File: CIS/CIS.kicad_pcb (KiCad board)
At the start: 8 copper layers, 88 parts, among them K1 K_0043, P1 K_0021, P2 K_0021, P7 K_0021, U1 U_0005, U10 U_0049, U11 U_0049, U14 U_0101, U15 U_0005, U16 U_0049, U17 U_0049, U2 STM32H745IIKx, U8 U_0049, U9 U_0049

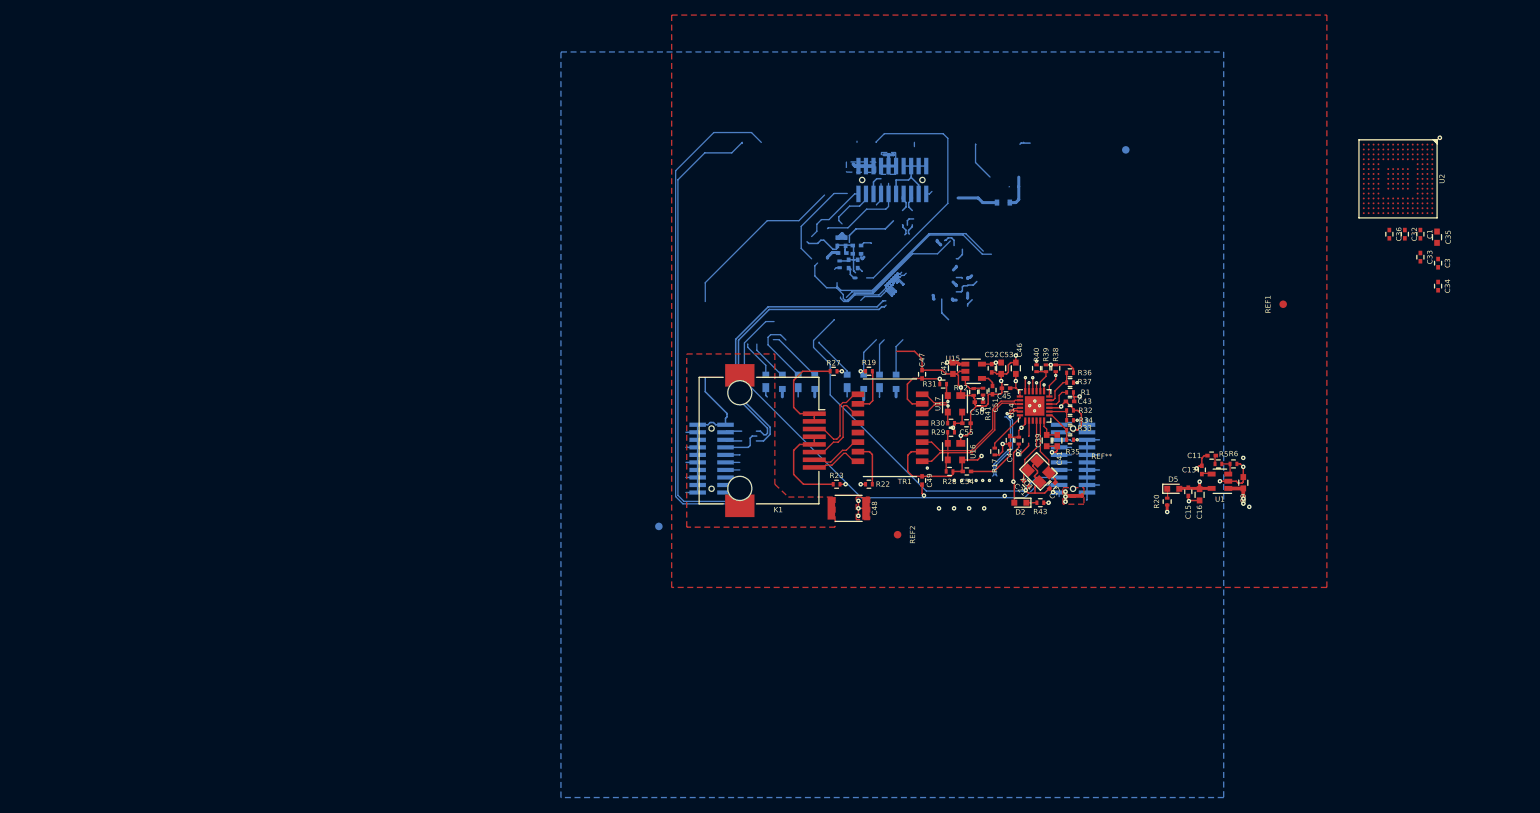
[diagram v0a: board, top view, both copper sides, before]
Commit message: Place components and route POWER + ETHERNET
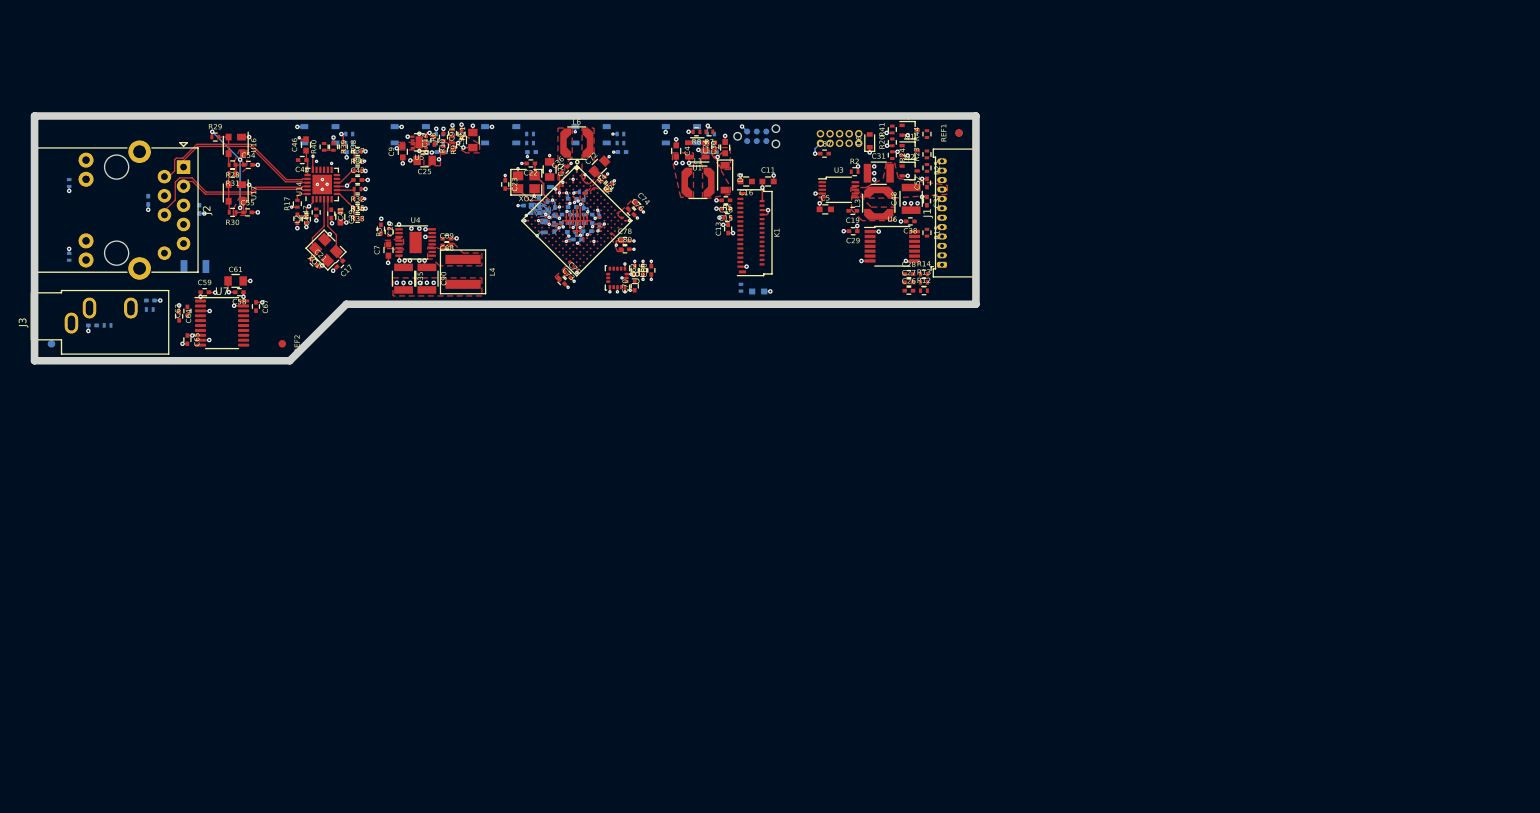
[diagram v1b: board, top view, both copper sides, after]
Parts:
- removed C50: C_0002, DVB_Capacitors_Ceramic:C_0402
- removed C51: C_0001, DVB_Capacitors_Ceramic:C_0402
- removed D5: D_0001, DVB_LED:LED_0603-red
- removed P1, P2, P7: K_0021, DVB_Connectors:K_MLE-110-01-G-DV-A
- removed REF**: VAL**, DVB_Mechanicals:DVBLOGO
- removed TR1: TR_0001, DVB_Transfo:LAN_8-13x7_P1.27
- removed U10, U11, U9: U_0049, DVB_SOT:SOT_143
- removed U15: U_0005, DVB_SOT:SOT_23-5
- added C14: C_0002, DVB_Capacitors_Ceramic:C_0402, F.Cu at (94.2, 75.8)
- added C18: C_0044, DVB_Capacitors_Ceramic:C_0402, F.Cu at (132.9, 83.7)
- added C19: C_0002, DVB_Capacitors_Ceramic:C_0402, F.Cu at (149.8, 85.1)
- added C20: C_0001, DVB_Capacitors_Ceramic:C_0402, F.Cu at (87.1, 87.5)
- added C22: C_0043, DVB_Capacitors_Ceramic:C_0402, F.Cu at (107.0, 78.8)
- added C23: C_0043, DVB_Capacitors_Ceramic:C_0402, F.Cu at (103.6, 81.6)
- added C26: C_0001, DVB_Capacitors_Ceramic:C_0402, F.Cu at (157.2, 95.7)
- added C27: C_0001, DVB_Capacitors_Ceramic:C_0402, F.Cu at (157.2, 94.6)
- added C28: C_0001, DVB_Capacitors_Ceramic:C_0402, F.Cu at (157.2, 93.5)
- added C29: C_0002, DVB_Capacitors_Ceramic:C_0402, F.Cu at (149.8, 87.8)
- added C30: C_0036, DVB_Capacitors_Ceramic:C_0603, F.Cu at (132.8, 76.7)
- added C31: C_0040, DVB_Capacitors_Ceramic:C_1210, F.Cu at (153.2, 80.1)
- added C37: C_0001, DVB_Capacitors_Ceramic:C_0402, F.Cu at (159.6, 83.8)
- added C38: C_0002, DVB_Capacitors_Ceramic:C_0402, F.Cu at (157.4, 86.5)
- added C4: C_0003, DVB_Capacitors_Ceramic:C_0603, F.Cu at (126.3, 77.2)
- added C40: C_0002, DVB_Capacitors_Ceramic:C_0402, B.Cu at (119.1, 77.3)
- added C5: C_0003, DVB_Capacitors_Ceramic:C_0603, F.Cu at (146.1, 84.9)
- added C56: C_0002, DVB_Capacitors_Ceramic:C_0402, B.Cu at (83.1, 77.3)
- added C57: C_0002, DVB_Capacitors_Ceramic:C_0402, B.Cu at (107.1, 77.3)
- added C58: C_0002, DVB_Capacitors_Ceramic:C_0402, F.Cu at (68.3, 95.9)
- added C59: C_0002, DVB_Capacitors_Ceramic:C_0402, F.Cu at (63.7, 95.9)
- added C60: C_0001, DVB_Capacitors_Ceramic:C_0402, F.Cu at (120.8, 93.0)
- added C61: C_0053, DVB_Capacitors_Ceramic:C_0805, F.Cu at (67.8, 94.4)
- added C62: C_0002, DVB_Capacitors_Ceramic:C_0402, F.Cu at (121.9, 93.0)
- added C63: C_0045, DVB_Capacitors_Ceramic:C_0402, F.Cu at (61.4, 98.4)
- added C64: C_0045, DVB_Capacitors_Ceramic:C_0402, F.Cu at (60.3, 99.1)
- added C65: C_0002, DVB_Capacitors_Ceramic:C_0402, F.Cu at (61.4, 102.2)
- added C66: C_0063, DVB_Capacitors_Ceramic:C_0402, F.Cu at (123.0, 93.0)
- added C67: C_0002, DVB_Capacitors_Ceramic:C_0402, F.Cu at (70.5, 97.8)
- added C68: C_, DVB_Capacitors_Ceramic:C_0402, B.Cu at (56.5, 97.0)
- added C69: C_, DVB_Capacitors_Ceramic:C_0402, B.Cu at (48.8, 100.3)
- added C7: C_0036, DVB_Capacitors_Ceramic:C_0603, F.Cu at (88.1, 90.3)
- added C70: C_0002, DVB_Capacitors_Ceramic:C_0402, F.Cu at (120.8, 95.1)
- added C71: C_0053, DVB_Capacitors_Ceramic:C_0805, F.Cu at (109.5, 79.6)
- added C72: C_0053, DVB_Capacitors_Ceramic:C_0805, F.Cu at (116.1, 79.2)
- added C73: C_0063, DVB_Capacitors_Ceramic:C_0402, F.Cu at (111.1, 94.4)
- added C74: C_0063, DVB_Capacitors_Ceramic:C_0402, F.Cu at (121.1, 84.4)
- added C75: C_0045, DVB_Capacitors_Ceramic:C_0402, F.Cu at (111.9, 93.6)
- added C76: C_0045, DVB_Capacitors_Ceramic:C_0402, F.Cu at (120.3, 85.2)
- added C77: C_0063, DVB_Capacitors_Ceramic:C_0402, B.Cu at (113.1, 86.2)
- added C78: C_0002, DVB_Capacitors_Ceramic:C_0402, F.Cu at (119.5, 89.1)
- added C79: C_0002, DVB_Capacitors_Ceramic:C_0402, B.Cu at (116.1, 86.4)
- added C80: C_0063, DVB_Capacitors_Ceramic:C_0402, F.Cu at (119.5, 90.2)
- added C81: C_0044, DVB_Capacitors_Ceramic:C_0402, B.Cu at (110.1, 87.3)
- added C82: C_0002, DVB_Capacitors_Ceramic:C_0402, B.Cu at (110.2, 85.2)
- added C83: C_0044, DVB_Capacitors_Ceramic:C_0402, B.Cu at (106.6, 84.4)
- added C84: C_0002, DVB_Capacitors_Ceramic:C_0402, B.Cu at (107.6, 85.4)
- added C85: C_0044, DVB_Capacitors_Ceramic:C_0402, B.Cu at (108.1, 83.9)
- added C86: C_0002, DVB_Capacitors_Ceramic:C_0402, B.Cu at (109.2, 84.4)
- added C87: C_0002, DVB_Capacitors_Ceramic:C_0402, F.Cu at (146.0, 77.5)
- added C88: C_0044, DVB_Capacitors_Ceramic:C_0402, F.Cu at (95.8, 88.8)
- added C89: C_0002, DVB_Capacitors_Ceramic:C_0402, F.Cu at (95.8, 89.7)
- added C90: C_0040, DVB_Capacitors_Ceramic:C_1210, F.Cu at (93.2, 94.1)
- added C91: C_0002, DVB_Capacitors_Ceramic:C_0402, F.Cu at (97.8, 74.9)
- added C92: C_0053, DVB_Capacitors_Ceramic:C_0805, F.Cu at (99.3, 75.7)
- added D1: D_0001, DVB_LED:LED_0603-red, B.Cu at (137.2, 95.8)
- added F1: F_0002, DVB_F:F_1206, B.Cu at (62.4, 92.5)
- added J1: Conn_01x12, Connector_Molex:Molex_PicoBlade_53048-1210_1x12_P1.25mm_Horizontal, F.Cu at (161.6, 85.4)
- added J2: RJ45_Abracon_ARJP11A-MASA-B-A-EMU2, Connector_RJ:RJ45_Abracon_ARJP11A-MA_Horizontal, F.Cu at (52.0, 85.0)
- added J3: SJ1-3533NG, Connector_Audio:Jack_3.5mm_CUI_SJ1-3533NG_Horizontal, F.Cu at (46.0, 100.0)
- added J4: DEBUG TAG, Connector:Tag-Connect_TC2030-IDC-NL_2x03_P1.27mm_Vertical, B.Cu at (137.0, 75.2)
- added L1: L_0011, DVB_Inductors:L_4018-Coilcraft, F.Cu at (129.2, 81.3)
- added L3: L_0009, DVB_Inductors:L_4018-Coilcraft, F.Cu at (153.2, 84.1)
- added L4: L_0002, DVB_Inductors:L_5030-Coilcraft, F.Cu at (98.0, 93.2)
- added L5: L_, DVB_Inductors:L_0603, B.Cu at (109.6, 81.2)
- added L6: L_, DVB_Inductors:L_4018-Coilcraft, F.Cu at (113.1, 76.1)
- added L7: L_0010, DVB_Inductors:L_0603, B.Cu at (108.8, 87.2)
- added P3: K_0023, DVB_Connectors:SHF-105-01-L-D-TH, B.Cu at (148.0, 75.5)
- added Q1: Q_0002, DVB_SOT:SOT_323-SC_70, F.Cu at (157.3, 77.1)
- added Q2: Q_0002, DVB_SOT:SOT_323-SC_70, F.Cu at (157.3, 79.8)
- added Q3: Q_0002, DVB_SOT:SOT_323-SC_70, F.Cu at (157.3, 74.4)
- added R10: NC, DVB_Resistors:R_0402, F.Cu at (96.6, 76.5)
- added R11: NC, DVB_Resistors:R_0402, F.Cu at (96.6, 74.8)
- added R12: R_0001, DVB_Resistors:R_0402, F.Cu at (159.2, 95.7)
- added R13: R_0001, DVB_Resistors:R_0402, F.Cu at (159.2, 94.6)
- added R14: R_0001, DVB_Resistors:R_0402, F.Cu at (159.2, 93.5)
- added R15: R_0134, DVB_Resistors:R_0402, F.Cu at (159.6, 88.0)
- added R16: R_0104, DVB_Resistors:R_0402, B.Cu at (134.9, 95.3)
- added R18: R_0005, DVB_Resistors:R_0402, B.Cu at (118.9, 76.1)
- added R2: R_0117, DVB_Resistors:R_0402, F.Cu at (150.0, 79.9)
- added R21: R_0020, DVB_Resistors:R_0402, B.Cu at (118.9, 74.9)
- added R24: R_0064, DVB_Resistors:R_0402, F.Cu at (155.0, 77.7)
- added R25: R_, DVB_Resistors:R_0402, F.Cu at (159.6, 79.4)
- added R26: R_0005, DVB_Resistors:R_0402, B.Cu at (130.9, 76.1)
- added R3: R_0030, DVB_Resistors:R_0402, F.Cu at (88.2, 87.9)
- added R44: R_, DVB_Resistors:R_0402, F.Cu at (159.6, 74.9)
- added R45: R_0005, DVB_Resistors:R_0402, B.Cu at (106.9, 76.1)
- added R46: R_0020, DVB_Resistors:R_0402, B.Cu at (106.9, 74.9)
- added R47: R_0020, DVB_Resistors:R_0402, F.Cu at (78.5, 85.3)
- added R48: R_0053, DVB_Resistors:R_0402, B.Cu at (45.7, 81.4)
- added R49: R_0053, DVB_Resistors:R_0402, B.Cu at (45.7, 91.2)
- added R50: R_, DVB_Resistors:R_0402, B.Cu at (50.8, 100.3)
- added R51: R_, DVB_Resistors:R_0402, B.Cu at (56.4, 98.2)
- added R52: NC, DVB_Resistors:R_0402, F.Cu at (116.5, 80.9)
- added R53: R_0020, DVB_Resistors:R_0402, B.Cu at (113.9, 82.6)
- added R7: R_0107, DVB_Resistors:R_0402, F.Cu at (130.7, 74.6)
- added R8: R_0108, DVB_Resistors:R_0402, F.Cu at (129.0, 74.6)
- added R9: R_0102, DVB_Resistors:R_0402, F.Cu at (95.4, 77.0)
- added SW1: SW_0003, DVB_Buttons:PTS810, B.Cu at (115.0, 75.0)
- added SW2: SW_0003, DVB_Buttons:PTS810, B.Cu at (91.0, 75.0)
- added SW3: SW_0003, DVB_Buttons:PTS810, B.Cu at (127.0, 75.0)
- added SW4: SW_0003, DVB_Buttons:PTS810, B.Cu at (79.0, 75.0)
- added SW5: SW_0003, DVB_Buttons:PTS810, B.Cu at (103.0, 75.0)
- added U3: U_0103, DVB_SSOP:MSOP_10-3x3_P0.5, F.Cu at (147.9, 82.3)
- added U4: U_1001, DVB_SSOP:MSOP_16-1EP_3x4_P0.5, F.Cu at (91.7, 89.3)
- added U5: U_0081, DVB_DFN:DFN-8-1EP_2x2_P0.5, F.Cu at (92.2, 76.0)
- added U6: U_0097, DVB_SSOP:TSSOP_14_4.4x5_P0.65, F.Cu at (155.0, 89.8)
- added U7: PCM5102, Package_SO:TSSOP-20_4.4x6.5mm_P0.65mm, F.Cu at (66.0, 100.0)
- added XO2: XO_0004, DVB_Clock:7M, F.Cu at (106.4, 81.3)
- C1, C3, C32, C33, C34, C47, C49: moved to B.Cu
- C11: value C_0002 -> C_0036; footprint DVB_Capacitors_Ceramic:C_0402 -> DVB_Capacitors_Ceramic:C_0603
- C13: value C_0001 -> C_0044
- C15: value C_0002 -> C_0044
- C24: value C_0045 -> C_0013; moved to F.Cu
- C25: value C_0045 -> C_0053; footprint DVB_Capacitors_Ceramic:C_0402 -> DVB_Capacitors_Ceramic:C_0805; moved to F.Cu
- C35: value C_0036 -> C_0040; footprint DVB_Capacitors_Ceramic:C_0603 -> DVB_Capacitors_Ceramic:C_1210
- C36: value C_0068 -> C_
- C41: value C_0037 -> C_0044; footprint DVB_Capacitors_Ceramic:C_0603 -> DVB_Capacitors_Ceramic:C_0402
- C42: value C_0037 -> C_0002; footprint DVB_Capacitors_Ceramic:C_0603 -> DVB_Capacitors_Ceramic:C_0402; moved to B.Cu
- C48: value C -> C_0040; footprint DVB_Capacitors_Ceramic:C_1812 -> DVB_Capacitors_Ceramic:C_1210
- C53: value C_0036 -> C_0002; footprint DVB_Capacitors_Ceramic:C_0603 -> DVB_Capacitors_Ceramic:C_0402; moved to B.Cu
- C9: value C_0037 -> C_0003
- D2: value D_0001 -> D_0021; footprint DVB_LED:LED_0603-red -> DVB_Diodes:D_SOD-123
- D6, R4: moved to F.Cu
- K1: value K_0043 -> K_9999; footprint mod:RJ45_SMD-15.7x16.4x13.4_noLeds -> DVB_Displays:OLED256x64-2P1_HOLE
- R19, R27: value R_0132 -> R_0005; moved to B.Cu
- R20: value R_0104 -> R_0064
- R22: value R_0132 -> R_0020; moved to B.Cu
- R23: value R_0132 -> R_
- R41: value R_0005 -> R_0064
- R42: value R_0002 -> R_0020; moved to B.Cu
- R43: value R_0104 -> R_0020; moved to B.Cu
- R5: value R_0005 -> R_0028
- R6: value R_0002 -> R_0121
- U1: value U_0005 -> U_0076
- U8: value U_0049 -> ICM-20602; footprint DVB_SOT:SOT_143 -> Package_LGA:LGA-16_3x3mm_P0.5mm_LayoutBorder3x5y; moved to F.Cu
- XO1: footprint DVB_Clock:XO_7M -> DVB_Clock:7M
- moved C35 137.3 mm to (90.1, 94.1)
- moved C9 119.9 mm to (90.0, 77.2)
- moved C34 114.4 mm to (113.2, 88.9), turned to 180 degrees
- moved R6 113.5 mm to (95.4, 75.3), turned to 90 degrees
- moved C3 113.1 mm to (114.6, 85.6), turned to 180 degrees
- moved C1 111.2 mm to (114.0, 84.2)
- moved C33 110.7 mm to (114.5, 87.8), turned to 180 degrees
- moved C36 109.8 mm to (111.5, 79.6), turned to 45 degrees
- moved C49 109.3 mm to (56.2, 83.7)
- moved U2 109.2 mm to (113.1, 86.4), turned to 315 degrees
- moved C32 108.5 mm to (114.6, 86.7), turned to 180 degrees
- moved R29 105.3 mm to (65.1, 75.3), turned to 0 degrees
- moved R43 104.0 mm to (82.9, 74.9)
- moved U16 103.8 mm to (67.8, 76.4), turned to 270 degrees
- moved C54 103.7 mm to (69.5, 79.0)
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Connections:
- C11 pad 1: GND -> +12V
- C11 pad 2: /SDRAM_POWER_V3 -> GND
- C13 pad 1: Net-(C13-Pad1) -> +3.3V
- C15 pad 1: RAM_+3.3V -> Net-(C15-Pad1)
- C16 pad 1: RAM_+3.3V -> Net-(C16-Pad1)
- C24 pad 1: Net-(C24-Pad1) -> +12V
- C24 pad 2: GND -> Net-(C24-Pad2)
- C25 pad 1: Net-(C25-Pad1) -> VERF+
- C35 pad 1: +3.3V -> GND
- C35 pad 2: GND -> +3.3V
- C36 pad 2: Net-(C36-Pad2) -> GND
- C42 pad 1: +5V -> /SW_UP
- C43 pad 1: ETH_+3.3V -> +3.3V
- C48 pad 1: DGND -> GND
- C48 pad 2: Net-(C48-Pad2) -> +5V
- C52 pad 1: ETH_+3.3V -> +5V
- C53 pad 1: ETH_+3.3V -> /SW_RIGHT
- C9 pad 1: +5V -> GND
- C9 pad 2: GND -> +3.3V
- D2 pad 1: Net-(D2-Pad1) -> +12V
- D2 pad 2: ETH_+3.3V -> Net-(D2-Pad2)
- K1 pad 1: /TX_+ -> Net-(K1-Pad1)
- K1 pad 2: /TX_- -> +12V
- K1 pad 3: /RX_+ -> Net-(C18-Pad1)
- K1 pad 4: Net-(K1-Pad4) -> Net-(C16-Pad1)
- K1 pad 5: Net-(K1-Pad4) -> Net-(C15-Pad1)
- K1 pad 6: /RX_- -> +12V
- K1 pad 8: Net-(K1-Pad7) -> +12V
- L2 pad 1: ETH_+3.3V -> +3.3V
- R19 pad 1: Net-(R19-Pad1) -> /SW_UP
- R19 pad 2: Net-(C48-Pad2) -> Net-(R19-Pad2)
- R20 pad 1: Net-(D5-Pad1) -> GND
- R20 pad 2: GND_LED -> /CIS_LED_R
- R22 pad 1: Net-(R22-Pad1) -> +3.3V
- R22 pad 2: Net-(C48-Pad2) -> /SW_UP
- R23 pad 1: Net-(K1-Pad4) -> /CIS_VLED_R
- R23 pad 2: Net-(C48-Pad2) -> Net-(Q1-Pad3)
- R27 pad 1: Net-(K1-Pad7) -> /SW_DOWN
- R27 pad 2: Net-(C48-Pad2) -> Net-(R27-Pad2)
- R32 pad 1: ETH_+3.3V -> +3.3V
- R33 pad 1: ETH_+3.3V -> +3.3V
- R34 pad 1: /RXD0 -> /RMII_RXD0
- R35 pad 2: /RXD1 -> /RMII_RXD1
- R36 pad 1: ETH_+3.3V -> +3.3V
- R37 pad 2: /ETH_CRS_DV -> /RMII_CRS_DV
- R38 pad 1: ETH_+3.3V -> +3.3V
- R38 pad 2: /ETH_MDIO -> /RMII_MDIO
- R39 pad 1: ETH_+3.3V -> +3.3V
- R40 pad 2: /ETH_REF_CLK -> /RMII_REF_CLK
- R41 pad 1: Net-(R41-Pad1) -> GND
- R41 pad 2: /ETH_POWER_V3 -> /CIS_LED_B
- R42 pad 1: Net-(R41-Pad1) -> +3.3V
- R42 pad 2: GND -> /SW_RIGHT
- R43 pad 1: Net-(D2-Pad1) -> +3.3V
- R43 pad 2: GND_LED -> /SW_DOWN
- R5 pad 1: Net-(R5-Pad1) -> GND
- R5 pad 2: /SDRAM_POWER_V3 -> Net-(K1-Pad7)
- R6 pad 1: Net-(R5-Pad1) -> Net-(R6-Pad1)
- U1 pad 1: +5V -> Net-(D2-Pad2)
- U1 pad 3: Net-(R5-Pad1) -> Net-(C24-Pad2)
- U1 pad 4: Net-(C13-Pad1) -> /12V_EN
- U1 pad 5: RAM_+3.3V -> +3.3V
- U14 pad 12: /ETH_MDIO -> /RMII_MDIO
- U14 pad 13: /ETH_MDC -> /RMII_MDC
- U14 pad 16: /ETH_TX_EN -> /RMII_TX_EN
- U14 pad 17: /ETH_TXD0 -> /RMII_TXD0
- U14 pad 18: /ETH_TXD1 -> /RMII_TXD1
- U14 pad 9: ETH_+3.3V -> +3.3V
- U2 pad A10: Net-(U2-PadA10) -> /FMC_D3
- U2 pad A11: Net-(U2-PadA11) -> /MEMS_FSYNC
- U2 pad A12: Net-(U2-PadA12) -> /SWD-CLK
- U2 pad A13: Net-(U2-PadA13) -> Net-(C72-Pad1)
- U2 pad A14: Net-(U2-PadA14) -> Net-(C72-Pad1)
- U2 pad A2: Net-(U2-PadA2) -> /OLED_RESET
- U2 pad A3: Net-(U2-PadA3) -> Net-(C72-Pad1)
- U2 pad A4: Net-(U2-PadA4) -> Net-(C72-Pad1)
- U2 pad A5: Net-(U2-PadA5) -> /DEBUG_TX
- U2 pad A6: Net-(U2-PadA6) -> (no net)
- U2 pad A7: Net-(U2-PadA7) -> /RMII_TX_EN
- U2 pad A8: Net-(U2-PadA8) -> (no net)
- U2 pad A9: Net-(U2-PadA9) -> /MEMS_SCLK
- U2 pad B1: Net-(U2-PadB1) -> /DAC_LRCK
- U2 pad B10: Net-(U2-PadB10) -> (no net)
- U2 pad B11: Net-(U2-PadB11) -> (no net)
- U2 pad B12: Net-(U2-PadB12) -> (no net)
- U2 pad B13: Net-(U2-PadB13) -> /SWD-IO
- U2 pad B14: Net-(U2-PadB14) -> (no net)
- U2 pad B15: Net-(U2-PadB15) -> /CIS_RS
- U2 pad B2: Net-(U2-PadB2) -> (no net)
- U2 pad B3: Net-(U2-PadB3) -> /MEMS_CS
- U2 pad B4: Net-(U2-PadB4) -> (no net)
- U2 pad B5: Net-(U2-PadB5) -> /DEBUG_RX
- U2 pad B6: Net-(U2-PadB6) -> (no net)
- U2 pad B7: Net-(U2-PadB7) -> /RMII_TXD0
- U2 pad B8: Net-(U2-PadB8) -> /FMC_NEx
- U2 pad B9: Net-(U2-PadB9) -> /FMC_NWE
- U2 pad C1: Net-(U2-PadC1) -> /DAC_FLT
- U2 pad C10: Net-(U2-PadC10) -> /FMC_D2
- U2 pad C11: Net-(U2-PadC11) -> (no net)
- U2 pad C12: Net-(U2-PadC12) -> (no net)
- U2 pad C13: Net-(U2-PadC13) -> (no net)
- U2 pad C14: Net-(U2-PadC14) -> (no net)
- U2 pad C15: Net-(U2-PadC15) -> (no net)
- U2 pad C3: Net-(U2-PadC3) -> /DAC_SCK
- U2 pad C4: Net-(U2-PadC4) -> (no net)
- U2 pad C6: Net-(U2-PadC6) -> (no net)
- U2 pad C7: Net-(U2-PadC7) -> /RMII_TXD1
- U2 pad C8: Net-(U2-PadC8) -> (no net)
- U2 pad C9: Net-(U2-PadC9) -> /FMC_NOE
- U2 pad D1: Net-(U2-PadD1) -> (no net)
- U2 pad D12: Net-(U2-PadD12) -> (no net)
- U2 pad D13: Net-(U2-PadD13) -> /CIS_CP
- U2 pad D14: Net-(U2-PadD14) -> /CIS_SP
- U2 pad D15: Net-(U2-PadD15) -> (no net)
- U2 pad D2: Net-(U2-PadD2) -> (no net)
- U2 pad D3: Net-(U2-PadD3) -> /DAC_BCK
- U2 pad D7: Net-(U2-PadD7) -> (no net)
- U2 pad D8: Net-(U2-PadD8) -> (no net)
- U2 pad D9: Net-(U2-PadD9) -> /DAC_DIN
- U2 pad E13: Net-(U2-PadE13) -> (no net)
- U2 pad E14: Net-(U2-PadE14) -> /CIS_VLED_R
- U2 pad E15: Net-(U2-PadE15) -> +3.3V
- U2 pad E2: (no net) -> +3.3V
- U2 pad E3: Net-(U2-PadE3) -> (no net)
- U2 pad F1: Net-(U2-PadF1) -> Net-(C36-Pad1)
- U2 pad F13: Net-(U2-PadF13) -> +3.3V
- U2 pad F14: Net-(U2-PadF14) -> (no net)
- U2 pad F15: Net-(U2-PadF15) -> (no net)
- U2 pad F2: Net-(U2-PadF2) -> GND
- U2 pad F3: Net-(U2-PadF3) -> (no net)
- U2 pad F4: Net-(U2-PadF4) -> /FMC_Ax
- U2 pad G12: Net-(U2-PadG12) -> /MEMS_INT
- U2 pad G13: Net-(U2-PadG13) -> (no net)
- U2 pad G14: Net-(U2-PadG14) -> (no net)
- U2 pad G15: Net-(U2-PadG15) -> (no net)
- U2 pad G2: Net-(U2-PadG2) -> Net-(C72-Pad1)
- U2 pad G3: Net-(U2-PadG3) -> (no net)
- U2 pad H1: Net-(U2-PadH1) -> /DAC_FMT
- U2 pad H13: Net-(U2-PadH13) -> (no net)
- U2 pad H14: Net-(U2-PadH14) -> /FMC_D0
- U2 pad H15: Net-(U2-PadH15) -> /CIS_VLED_G
- U2 pad H2: Net-(U2-PadH2) -> (no net)
- U2 pad H3: Net-(U2-PadH3) -> (no net)
- U2 pad H4: Net-(U2-PadH4) -> /12V_EN
- U2 pad J12: Net-(U2-PadJ12) -> /FMC_D1
- U2 pad J13: Net-(U2-PadJ13) -> (no net)
- U2 pad J15: Net-(U2-PadJ15) -> (no net)
- U2 pad J2: Net-(U2-PadJ2) -> (no net)
- U2 pad J3: Net-(U2-PadJ3) -> (no net)
- U2 pad J4: Net-(U2-PadJ4) -> /5V_EN
- U2 pad K13: Net-(U2-PadK13) -> (no net)
- U2 pad K14: Net-(U2-PadK14) -> /MEMS_MOSI
- U2 pad K15: Net-(U2-PadK15) -> /MEMS_MISO
- U2 pad K3: Net-(U2-PadK3) -> (no net)
- U2 pad L13: Net-(U2-PadL13) -> (no net)
- U2 pad L14: Net-(U2-PadL14) -> (no net)
- U2 pad L15: Net-(U2-PadL15) -> (no net)
- U2 pad L2: Net-(U2-PadL2) -> (no net)
- U2 pad L3: Net-(U2-PadL3) -> /RMII_MDC
- U2 pad L4: Net-(U2-PadL4) -> VERF-
- U2 pad M1: Net-(U2-PadM1) -> /DAC_XSMT
- U2 pad M11: Net-(U2-PadM11) -> /DAC_DEMP
- U2 pad M12: Net-(U2-PadM12) -> /SW_LEFT
- U2 pad M13: Net-(U2-PadM13) -> (no net)
- U2 pad M14: Net-(U2-PadM14) -> (no net)
- U2 pad M15: Net-(U2-PadM15) -> (no net)
- U2 pad M2: Net-(U2-PadM2) -> (no net)
- U2 pad M3: Net-(U2-PadM3) -> VERF+
- U2 pad M7: Net-(U2-PadM7) -> /RMII_RXD1
- U2 pad M8: Net-(U2-PadM8) -> (no net)
- U2 pad N1: Net-(U2-PadN1) -> (no net)
- U2 pad N10: Net-(U2-PadN10) -> (no net)
- U2 pad N11: Net-(U2-PadN11) -> (no net)
- U2 pad N12: Net-(U2-PadN12) -> (no net)
- U2 pad N13: Net-(U2-PadN13) -> (no net)
- U2 pad N14: Net-(U2-PadN14) -> (no net)
- U2 pad N15: Net-(U2-PadN15) -> /CIS_VLED_B
- U2 pad N2: Net-(U2-PadN2) -> /CIS_ADC_3
- U2 pad N4: Net-(U2-PadN4) -> (no net)
- U2 pad N5: Net-(U2-PadN5) -> (no net)
- U2 pad N6: Net-(U2-PadN6) -> /RMII_CRS_DV
- U2 pad N7: Net-(U2-PadN7) -> (no net)
- U2 pad N8: Net-(U2-PadN8) -> /FMC_D5
- U2 pad N9: Net-(U2-PadN9) -> (no net)
- U2 pad P1: Net-(U2-PadP1) -> (no net)
- U2 pad P10: Net-(U2-PadP10) -> (no net)
- U2 pad P11: Net-(U2-PadP11) -> (no net)
- U2 pad P12: Net-(U2-PadP12) -> /SW_RIGHT
- U2 pad P13: Net-(U2-PadP13) -> /SW_DOWN
- U2 pad P14: Net-(U2-PadP14) -> /SW_OK
- U2 pad P15: Net-(U2-PadP15) -> /LED1
- U2 pad P2: Net-(U2-PadP2) -> /RMII_REF_CLK
- U2 pad P3: Net-(U2-PadP3) -> /CIS_ADC_2
- U2 pad P4: Net-(U2-PadP4) -> (no net)
- U2 pad P5: Net-(U2-PadP5) -> (no net)
- U2 pad P6: Net-(U2-PadP6) -> (no net)
- U2 pad P7: Net-(U2-PadP7) -> (no net)
- U2 pad P8: Net-(U2-PadP8) -> (no net)
- U2 pad P9: Net-(U2-PadP9) -> /FMC_D4
- U2 pad R10: Net-(U2-PadR10) -> (no net)
- U2 pad R11: Net-(U2-PadR11) -> /FMC_D6
- U2 pad R12: Net-(U2-PadR12) -> /SW_UP
- U2 pad R13: Net-(U2-PadR13) -> Net-(C72-Pad1)
- U2 pad R14: Net-(U2-PadR14) -> Net-(C72-Pad1)
- U2 pad R2: Net-(U2-PadR2) -> /RMII_MDIO
- U2 pad R3: Net-(U2-PadR3) -> /CIS_ADC_1
- U2 pad R4: Net-(U2-PadR4) -> (no net)
- U2 pad R5: Net-(U2-PadR5) -> (no net)
- U2 pad R6: Net-(U2-PadR6) -> /RMII_RXD0
- U2 pad R7: Net-(U2-PadR7) -> (no net)
- U2 pad R8: Net-(U2-PadR8) -> (no net)
- U2 pad R9: Net-(U2-PadR9) -> /FMC_D7
- U8 pad 1: GND -> +3.3V
- U8 pad 2: /SDIO-D3 -> /MEMS_SCLK
- U8 pad 3: /SDIO-D2 -> /MEMS_MOSI
- U8 pad 4: SD_+3.3V -> /MEMS_MISO
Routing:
- net /I2C_INTERNAL_SDA: track 189.0 -> 0.00 mm
- net +3.3V: track 116.5 -> 303.7 mm, vias 0 -> 53
- net GND: track 733.0 -> 581.9 mm, vias 27 -> 139
- net /DCMI_IO_POWER: track 144.0 -> 0.00 mm
- net /I2C_INTERNAL_SCL: track 104.7 -> 0.00 mm
- net /RST: track 103.7 -> 0.00 mm, vias 2 -> 0
- net /USART-TX: track 63.6 -> 0.00 mm
- net SD_+3.3V: track 62.1 -> 0.00 mm
- net /MCU_WAKE_UP: track 59.1 -> 0.00 mm
- net ETH_+3.3V: track 50.7 -> 0.00 mm, vias 4 -> 0
- net /MODEM_RINGING: track 49.7 -> 0.00 mm, vias 1 -> 0
- net /WAKEUP_BROADCAST: track 48.5 -> 0.00 mm
- net /MODEM_RESET: track 48.2 -> 0.00 mm, vias 1 -> 0
- net /MAIN_POWER_GOOD_5V: track 47.2 -> 0.00 mm, vias 1 -> 0
- net /USART-RX: track 46.4 -> 0.00 mm
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- added copper zone on F.Cu, net +12V
- added copper zone on F.Cu, net +15
- added copper zone on F.Cu, net +3.3V
- added copper zone on F.Cu, net Net-(C19-Pad1)
- added copper zone on F.Cu, net Net-(C36-Pad1)
- added copper zone on F.Cu, net Net-(C44-Pad1)
- added copper zone on F.Cu, net Net-(C72-Pad1)
- added copper zone on POWER.Cu, net Net-(C72-Pad1)
- added copper zone on B.Cu, net Net-(C81-Pad2)
- added copper zone on F.Cu, net Net-(C89-Pad2)
- added copper zone on F.Cu, net Net-(D2-Pad2)
- added copper zone on F.Cu, net Net-(R4-Pad1)
- added copper zone on B.Cu, net VERF+
- added copper zone on F.Cu, net VERF+
- added copper zone on B.Cu, net VERF-
- added copper zone on F.Cu, net VERF-
- removed copper zone on B.Cu, net +3.3V
- removed copper zone on VDD.Cu, net +3.3V
- removed copper zone on B.Cu, net +5V
- removed copper zone on VDD.Cu, net +5V
- removed copper zone on F.Cu, net DGND
- removed copper zone on VDD.Cu, net ETH_+3.3V
- removed copper zone on B.Cu, net GND
- removed copper zone on F.Cu, net GND
- removed copper zone on GND.Cu, net GND
- removed copper zone on Interne1.Cu, net GND
- removed copper zone on Interne2.Cu, net GND
- removed copper zone on Interne3.Cu, net GND
- removed copper zone on Interne4.Cu, net GND
- removed copper zone on VDD.Cu, net Net-(C44-Pad1)
- removed copper zone on F.Cu, net Net-(C48-Pad2)
- removed copper zone on GND.Cu, net Net-(C48-Pad2)
- removed copper zone on VDD.Cu, net RAM_+3.3V
- removed copper zone on VDD.Cu, net SD_+3.3V
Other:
- board outline added: 125 x 32.5 mm
- copper layers 8 -> 6
- net class +5V removed
- net class DCMI removed
- net class FMC removed
- net class POWER added: clearance 0.091, trace_width 0.5, via_dia 0.6, via_drill 0.25
- net class SDIO removed
- net class USB_FS removed
- net class USB_HS removed
- net class VDD removed
- board text removed: "HM v3.3.0"
- board text removed: "Manufacturer : EuroCircuit PCB Thickness : 1mm Stack Up : 8 Layers Sig Ext : -------- 0,012 mm # 0,14 mm # GND : -------- 0,012 mm # 0,10 mm # Sig Int : -------- 0,012 mm # 0,14 mm # Sig Int : -------- 0,012 mm # 0,10 mm # Sig Int : -------- 0,012 mm # 0,14 mm # Sig Int : -------- 0,012 mm # 0,10 mm # Vdd : -------- 0,012 mm # 0,14 mm # Sig Ext : -------- 0,012 mm Impedance : Ethernet : Target : 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"

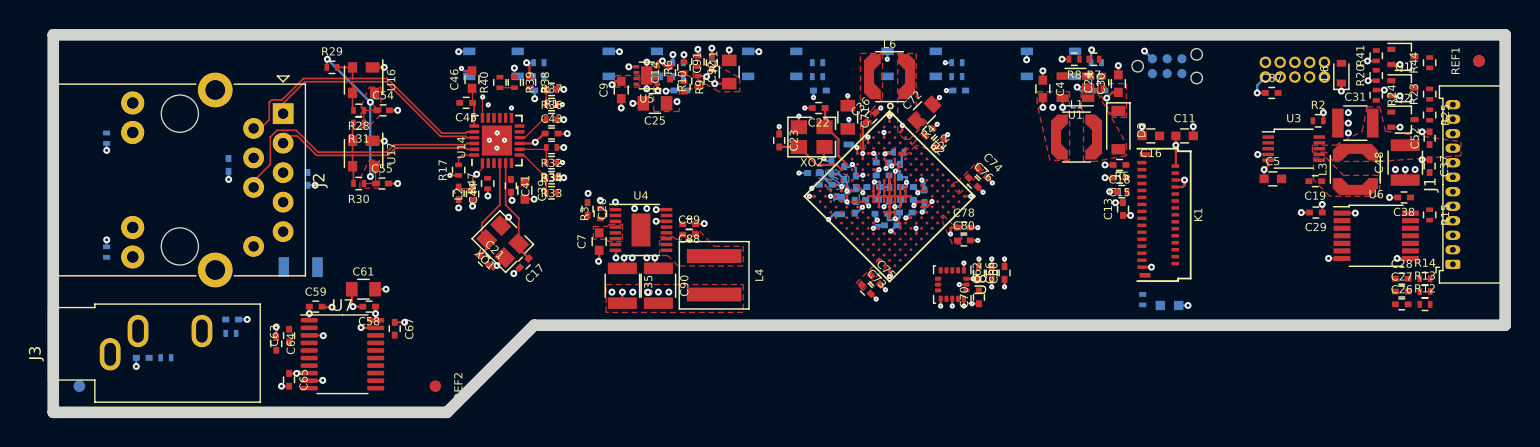
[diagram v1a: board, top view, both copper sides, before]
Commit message: First autoroute succes
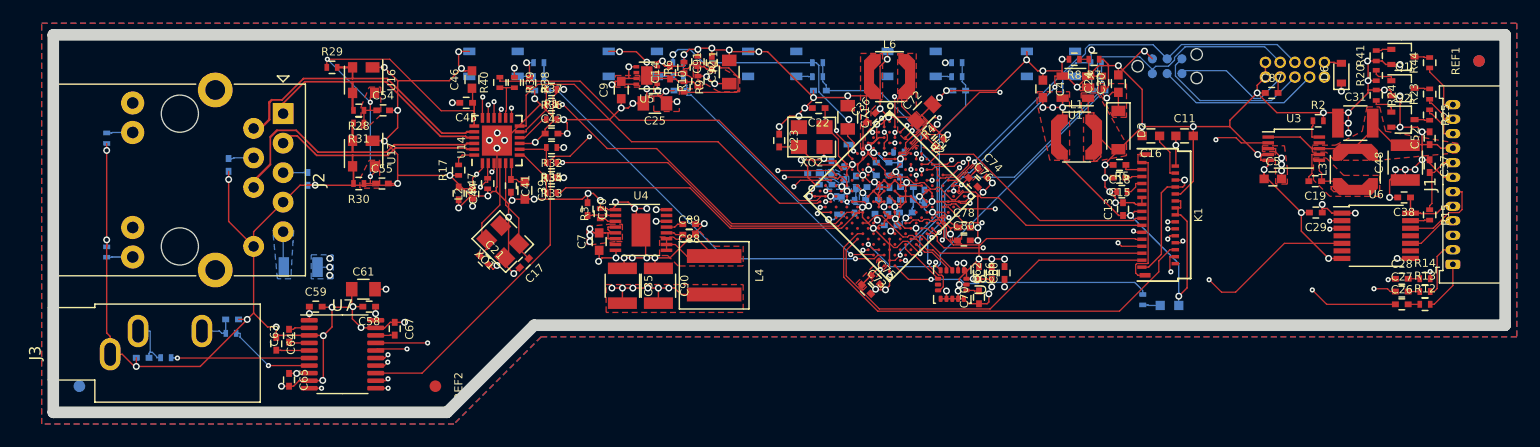
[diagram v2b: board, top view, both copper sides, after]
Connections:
- U2 pad F15: (no net) -> /12V_EN
- U2 pad G12: /MEMS_INT -> (no net)
- U2 pad G15: (no net) -> /5V_EN
- U2 pad H4: /12V_EN -> (no net)
- U2 pad J4: /5V_EN -> (no net)
- U2 pad L14: (no net) -> /MEMS_INT
- U2 pad M11: /DAC_DEMP -> (no net)
- U2 pad R4: (no net) -> /DAC_DEMP
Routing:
- net +15: track 0.00 -> 112.5 mm, vias 0 -> 9
- net /RST: track 0.00 -> 94.5 mm, vias 0 -> 2
- net GND: track 581.9 -> 513.1 mm, vias 139 -> 137
- net /CIS_VLED_B: track 0.00 -> 60.6 mm, vias 0 -> 1
- net /DAC_BCK: track 0.00 -> 58.2 mm, vias 0 -> 2
- net /DAC_SCK: track 0.00 -> 57.6 mm, vias 0 -> 2
- net Net-(C72-Pad1): track 1.14 -> 57.4 mm, vias 2 -> 5
- net /DAC_FLT: track 0.00 -> 55.8 mm, vias 0 -> 2
- net /CIS_ADC_1: track 0.00 -> 54.3 mm, vias 0 -> 2
- net /DAC_DIN: track 0.00 -> 54.0 mm, vias 0 -> 2
- net /CIS_ADC_3: track 0.00 -> 54.0 mm, vias 0 -> 2
- net /DAC_LRCK: track 0.00 -> 53.8 mm, vias 0 -> 2
- net /CIS_ADC_2: track 0.00 -> 53.2 mm, vias 0 -> 2
- net /CIS_VLED_G: track 0.00 -> 53.1 mm, vias 0 -> 1
- net /DEBUG_RX: track 0.00 -> 51.8 mm, vias 0 -> 1
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- added copper zone on B.Cu, net +15
- added copper zone on POWER.Cu, net +15
- added copper zone on POWER.Cu, net +3.3V
- added copper zone on B.Cu, net GND
- added copper zone on F.Cu, net GND
- added copper zone on GND.Cu, net GND
- added copper zone on In1.Cu, net GND
- added copper zone on In2.Cu, net GND
- added copper zone on B.Cu, net Net-(F1-Pad1)
- removed copper zone on POWER.Cu, net Net-(C72-Pad1)
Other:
- net class Default: via_drill 0.1 -> 0.2
- net class ETH: via_drill 0.1 -> 0.2
- net class GND: clearance 0.091 -> 0.125; trace_width 0.2 -> 0.125; via_dia 0.45 -> 0.6; via_drill 0.1 -> 0.35
- net class POWER: clearance 0.091 -> 0.125; trace_width 0.5 -> 0.125; via_drill 0.25 -> 0.35

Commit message: DRC succes!
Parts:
- moved R11 4.03 mm to (100.3, 76.4)
- moved C14 4.03 mm to (97.9, 77.3)
- moved C9 4.03 mm to (93.7, 78.8)
- moved C91 4.03 mm to (101.5, 76.5)
- moved C92 4.03 mm to (103.0, 77.3)
- moved R10 4.03 mm to (100.3, 78.1)
- moved U5 4.03 mm to (95.9, 77.6)
- moved R6 4.03 mm to (99.1, 76.9)
- moved C25 4.03 mm to (96.6, 80.0)
- moved R9 4.03 mm to (99.1, 78.6)
- moved R15 0.15 mm to (159.6, 87.8)
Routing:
- net GND: track 513.1 -> 143.6 mm, vias 137 -> 141
- net +3.3V: track 284.9 -> 83.4 mm, vias 52 -> 53
- net Net-(R6-Pad1): track 13.9 -> 6.47 mm, vias 0 -> 2
- net VERF+: track 30.9 -> 24.2 mm
- net Net-(C72-Pad1): track 57.4 -> 51.3 mm
- net VERF-: track 23.9 -> 18.3 mm
- net /OLED_RESET: track 35.8 -> 31.4 mm
- net /RMII_TX_EN: track 41.3 -> 45.2 mm
- net +5V: track 34.6 -> 31.0 mm
- net /DEBUG_TX: track 49.4 -> 52.3 mm
- net /CIS_SP_TTL: track 7.42 -> 5.52 mm, vias 0 -> 1
- net Net-(C36-Pad1): track 10.5 -> 8.75 mm
- net /RMII_REF_CLK: track 32.8 -> 34.4 mm
- net +15: track 112.5 -> 114.1 mm
- net /DAC_SCK: track 57.6 -> 56.1 mm
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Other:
- net class AUDIO added: clearance 0.091, trace_width 0.2, via_dia 0.6, via_drill 0.35
- net class GND: clearance 0.125 -> 0.091
- net class POWER: clearance 0.125 -> 0.091
- net class VREF added: clearance 0.091, trace_width 0.4, via_dia 0.6, via_drill 0.35

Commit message: Update 3d model
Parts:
- added REF2: CircleWhite1mm, DVB_Fiducials:REF_1mm_Top, F.Cu at (43.4, 74.8)
- added REF4: CircleWhite1mm, DVB_Fiducials:REF_1mm, B.Cu at (74.0, 102.8)
- J1: footprint Connector_Molex:Molex_PicoBlade_53048-1210_1x12_P1.25mm_Horizontal -> DVB_Connectors:Molex_PicoBlade_53048-1210_1x12_P1.25mm_Horizontal
- J2: footprint Connector_RJ:RJ45_Abracon_ARJP11A-MA_Horizontal -> DVB_Connectors:RJ45_Abracon_ARJP11A-MA_Horizontal
- J3: footprint Connector_Audio:Jack_3.5mm_CUI_SJ1-3533NG_Horizontal -> DVB_Connectors:Jack_3.5mm_CUI_SJ1-3533NG_Horizontal
- K1: footprint DVB_Displays:OLED256x64-2P1_HOLE -> DVB_Displays:OLED256x64-2P1_HOLE_TE_3-2328724-1‎
- U14: footprint DVB_QFN_DFN:QFN-24-1EP_4x4mm_Pitch0.5mm -> DVB_QFN:QFN-24-1EP_4x4mm_Pitch0.5mm
- U8: footprint Package_LGA:LGA-16_3x3mm_P0.5mm_LayoutBorder3x5y -> DVB_LGA:LGA-16_3x3mm_P0.5mm_LayoutBorder3x5y
- moved C15 19.6 mm to (129.2, 65.6)
- moved C18 19.6 mm to (129.2, 64.5)
- moved C13 19.6 mm to (129.5, 68.3)
- moved R5 19.6 mm to (129.4, 66.8)
- moved J2 10.6 mm to (60.9, 79.3)
- moved J1 6.86 mm to (161.6, 92.3)
- moved K1 5.00 mm to (131.3, 88.0)
- moved C26 3.80 mm to (153.4, 95.7)
- moved C27 3.80 mm to (153.4, 94.6)
- moved C28 3.80 mm to (153.4, 93.5)
- moved R12 3.80 mm to (155.4, 95.7)
- moved R13 3.80 mm to (155.4, 94.6)
- moved R14 3.80 mm to (155.4, 93.5)
- moved C16 3.20 mm to (132.6, 80.1)
- moved C30 3.20 mm to (129.8, 75.6)
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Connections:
- J2 pad 15: Net-(J2-Pad15) -> GND
- U2 pad E14: /CIS_VLED_R -> /CIS_LED_R
- U2 pad H15: /CIS_VLED_G -> /CIS_LED_G
- U2 pad N15: /CIS_VLED_B -> /CIS_LED_B
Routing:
- net /CIS_VLED_B: track 60.7 -> 0.65 mm, vias 1 -> 0
- net /CIS_LED_B: track 1.34 -> 53.3 mm, vias 0 -> 2
- net /CIS_VLED_G: track 53.5 -> 2.48 mm, vias 1 -> 0
- net /CIS_VLED_R: track 51.3 -> 2.74 mm, vias 1 -> 0
- net /CIS_LED_G: track 2.12 -> 46.3 mm, vias 0 -> 2
- net /CIS_LED_R: track 2.08 -> 44.1 mm, vias 0 -> 2
- net GND: track 143.6 -> 111.1 mm, vias 141 -> 133
- net /DEBUG_RX: track 51.8 -> 28.8 mm
- net /FMC_D5: track 25.9 -> 8.34 mm
- net +3.3V: track 83.4 -> 66.0 mm, vias 53 -> 49
- net /FMC_NEx: track 21.8 -> 4.95 mm
- net Net-(J2-Pad15): track 15.5 -> 0.00 mm
- net /FMC_Ax: track 25.7 -> 10.9 mm
- net /FMC_D1: track 22.3 -> 9.95 mm
- net Net-(K1-Pad1): track 12.3 -> 0.00 mm
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- added copper zone on B.Cu, net +3.3V
- added copper zone on POWER.Cu, net +5V
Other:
- board text added: "2020 - v1.0.0"
